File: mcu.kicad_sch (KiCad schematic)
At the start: 36 parts, among them J17 CAN, J19 Conn_ARM_JTAG_SWD_10, J20 Conn_ARM_JTAG_SWD_10, J21 Conn_01x04_Pin, SW1 RESET, SW2 BOOT, U17 HDC1080, U18 SN65HVD230, U3 STM32U575RGTx

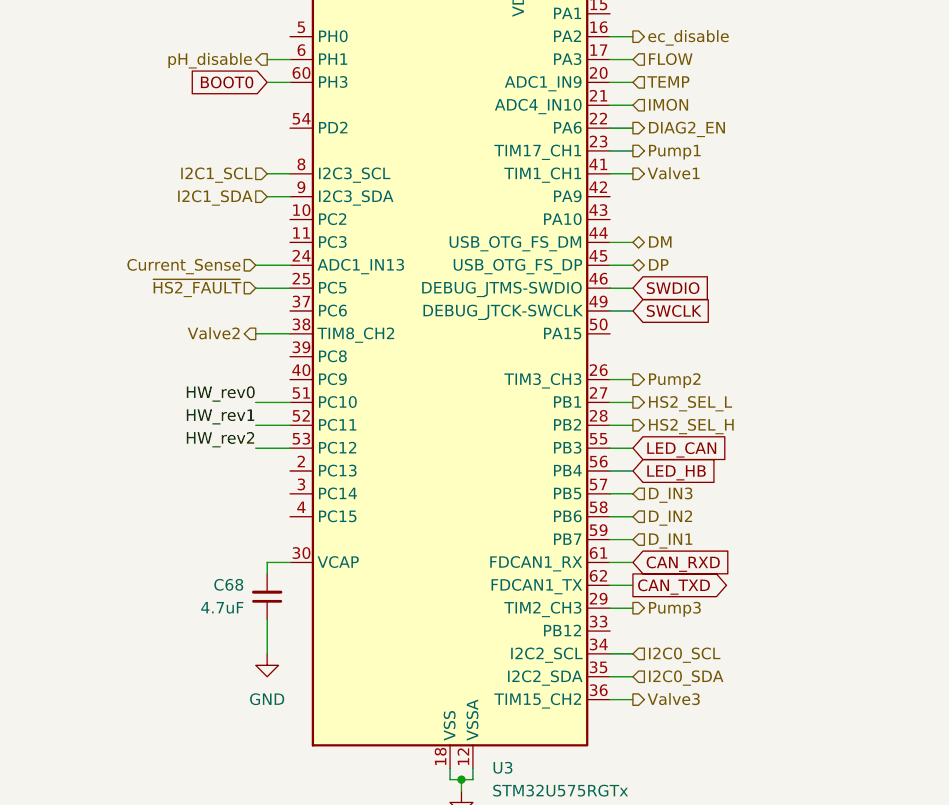
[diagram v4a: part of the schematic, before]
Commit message: Replace the last 2 of the highside outputs with TPS4H160B
Closes #50
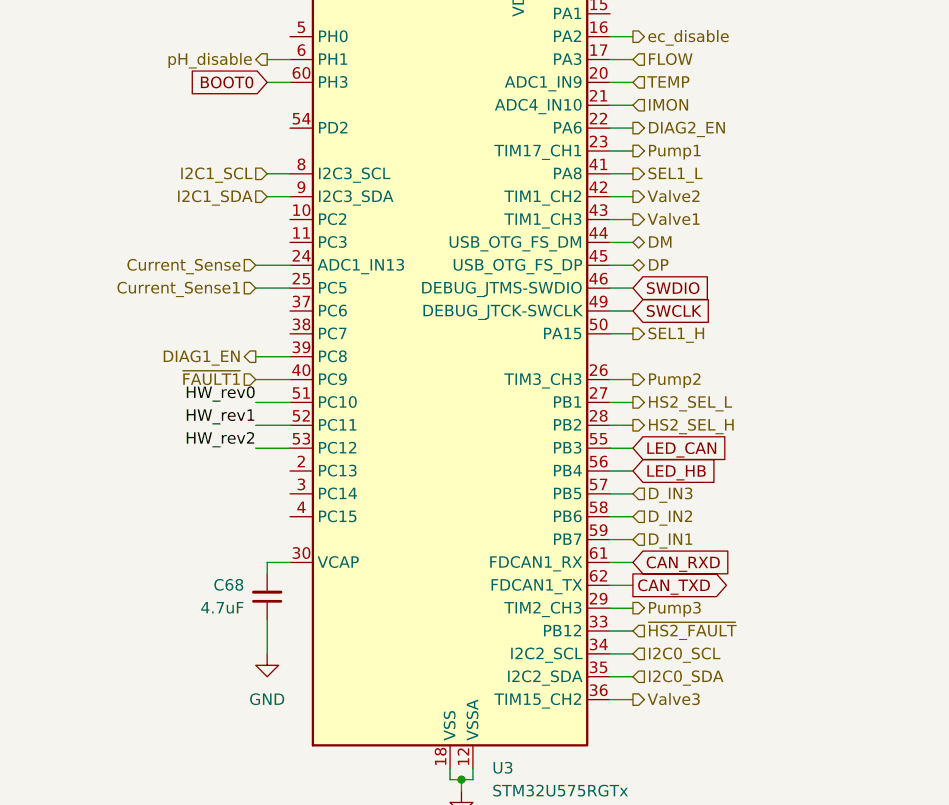
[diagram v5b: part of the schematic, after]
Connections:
- net Valve1: now also U3.43 (PA10); no longer U3.41 (PA8)
- net Valve2: now also U3.42 (PA9); no longer U3.38 (PC7)
- net ~{HS2_FAULT}: now also U3.33 (PB12); no longer U3.25 (PC5)
- net DIAG1_EN: now reaches U3.39 (PC8)
- net ~{FAULT1}: now reaches U3.40 (PC9)
- net SEL1_H: now reaches U3.50 (PA15)
- new net Current_Sense1: U3.25 (PC5)
- new net SEL1_L: U3.41 (PA8)
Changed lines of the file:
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@@
 		)
 	)
+	(wire
+		(pts
+			(xy 41.91 82.55) (xy 45.72 82.55)
+		)
+		(stroke
+			(width 0)
+			(type default)
+		)
+	)
 	(polyline
 		(pts
@@
 	(wire
 		(pts
-			(xy 41.91 77.47) (xy 45.72 77.47)
-		)
-		(stroke
-			(width 0)
-			(type default)
-		)
-	)
-	(wire
-		(pts
 			(xy 53.34 177.8) (xy 53.34 181.61)
 		)
@@
 	(wire
 		(pts
+			(xy 81.28 77.47) (xy 83.82 77.47)
+		)
+		(stroke
+			(width 0)
+			(type default)
+		)
+	)
+	(wire
+		(pts
 			(xy 43.18 59.69) (xy 45.72 59.69)
 		)
@@
 	(wire
 		(pts
+			(xy 41.91 80.01) (xy 45.72 80.01)
+		)
+		(stroke
+			(width 0)
+			(type default)
+		)
+	)
+	(wire
+		(pts
 			(xy 83.82 69.85) (xy 81.28 69.85)
 		)
@@
 	(wire
 		(pts
+			(xy 81.28 110.49) (xy 83.82 110.49)
+		)
+		(stroke
+			(width 0)
+			(type default)
+		)
+	)
+	(wire
+		(pts
 			(xy 83.82 97.79) (xy 81.28 97.79)
 		)
@@
 	(wire
 		(pts
+			(xy 81.28 62.23) (xy 83.82 62.23)
+		)
+		(stroke
+			(width 0)
+			(type default)
+		)
+	)
+	(wire
+		(pts
 			(xy 83.82 44.45) (xy 81.28 44.45)
 		)
@@
 	(wire
 		(pts
+			(xy 81.28 64.77) (xy 83.82 64.77)
+		)
+		(stroke
+			(width 0)
+			(type default)
+		)
+	)
+	(wire
+		(pts
 			(xy 63.5 125.73) (xy 63.5 127)
 		)
@@
 		)
 	)
+	(hierarchical_label "SEL1_L"
+		(shape output)
+		(at 83.82 59.69 0)
+		(effects
+			(font
+				(size 1.27 1.27)
+			)
+			(justify left)
+		)
+	)
 	(hierarchical_label "I2C0_SDA"
 		(shape input)
@@
 		)
 	)
+	(hierarchical_label "DIAG1_EN"
+		(shape output)
+		(at 41.91 80.01 180)
+		(effects
+			(font
+				(size 1.27 1.27)
+			)
+			(justify right)
+		)
+	)
 	(hierarchical_label "HS2_SEL_H"
 		(shape output)
@@
 	(hierarchical_label "~{HS2_FAULT}"
 		(shape input)
-		(at 41.91 72.39 180)
+		(at 83.82 110.49 0)
 		(effects
 			(font
 				(size 1.27 1.27)
 			)
-			(justify right)
+			(justify left)
 		)
 	)
@@
 		)
 	)
+	(hierarchical_label "~{FAULT1}"
+		(shape input)
+		(at 41.91 82.55 180)
+		(effects
+			(font
+				(size 1.27 1.27)
+			)
+			(justify right)
+		)
+	)
 	(hierarchical_label "Valve2"
 		(shape output)
-		(at 41.91 77.47 180)
+		(at 83.82 62.23 0)
 		(effects
 			(font
 				(size 1.27 1.27)
 			)
-			(justify right)
+			(justify left)
 		)
 	)
@@
 		)
 	)
+	(hierarchical_label "SEL1_H"
+		(shape output)
+		(at 83.82 77.47 0)
+		(effects
+			(font
+				(size 1.27 1.27)
+			)
+			(justify left)
+		)
+	)
 	(hierarchical_label "IMON"
 		(shape input)
@@
 	(hierarchical_label "Valve1"
 		(shape output)
-		(at 83.82 59.69 0)
+		(at 83.82 64.77 0)
 		(effects
 			(font
@@
 		)
 	)
+	(hierarchical_label "Current_Sense1"
+		(shape input)
+		(at 41.91 72.39 180)
+		(effects
+			(font
+				(size 1.27 1.27)
+			)
+			(justify right)
+		)
+	)
 	(symbol
 		(lib_id "power:+3.3V")
@@
 		)
 		(pin "38"
-			(alternate "TIM8_CH2")
+			(alternate "PC7")
 		)
 		(pin "56"
@@
 		)
 		(pin "42"
-			(alternate "PA9")
+			(alternate "TIM1_CH2")
 		)
 		(pin "29"
@@
 		)
 		(pin "43"
-			(alternate "PA10")
+			(alternate "TIM1_CH3")
 		)
 		(pin "8"
@@
 		)
 		(pin "41"
-			(alternate "TIM1_CH1")
+			(alternate "PA8")
 		)
 		(pin "26"

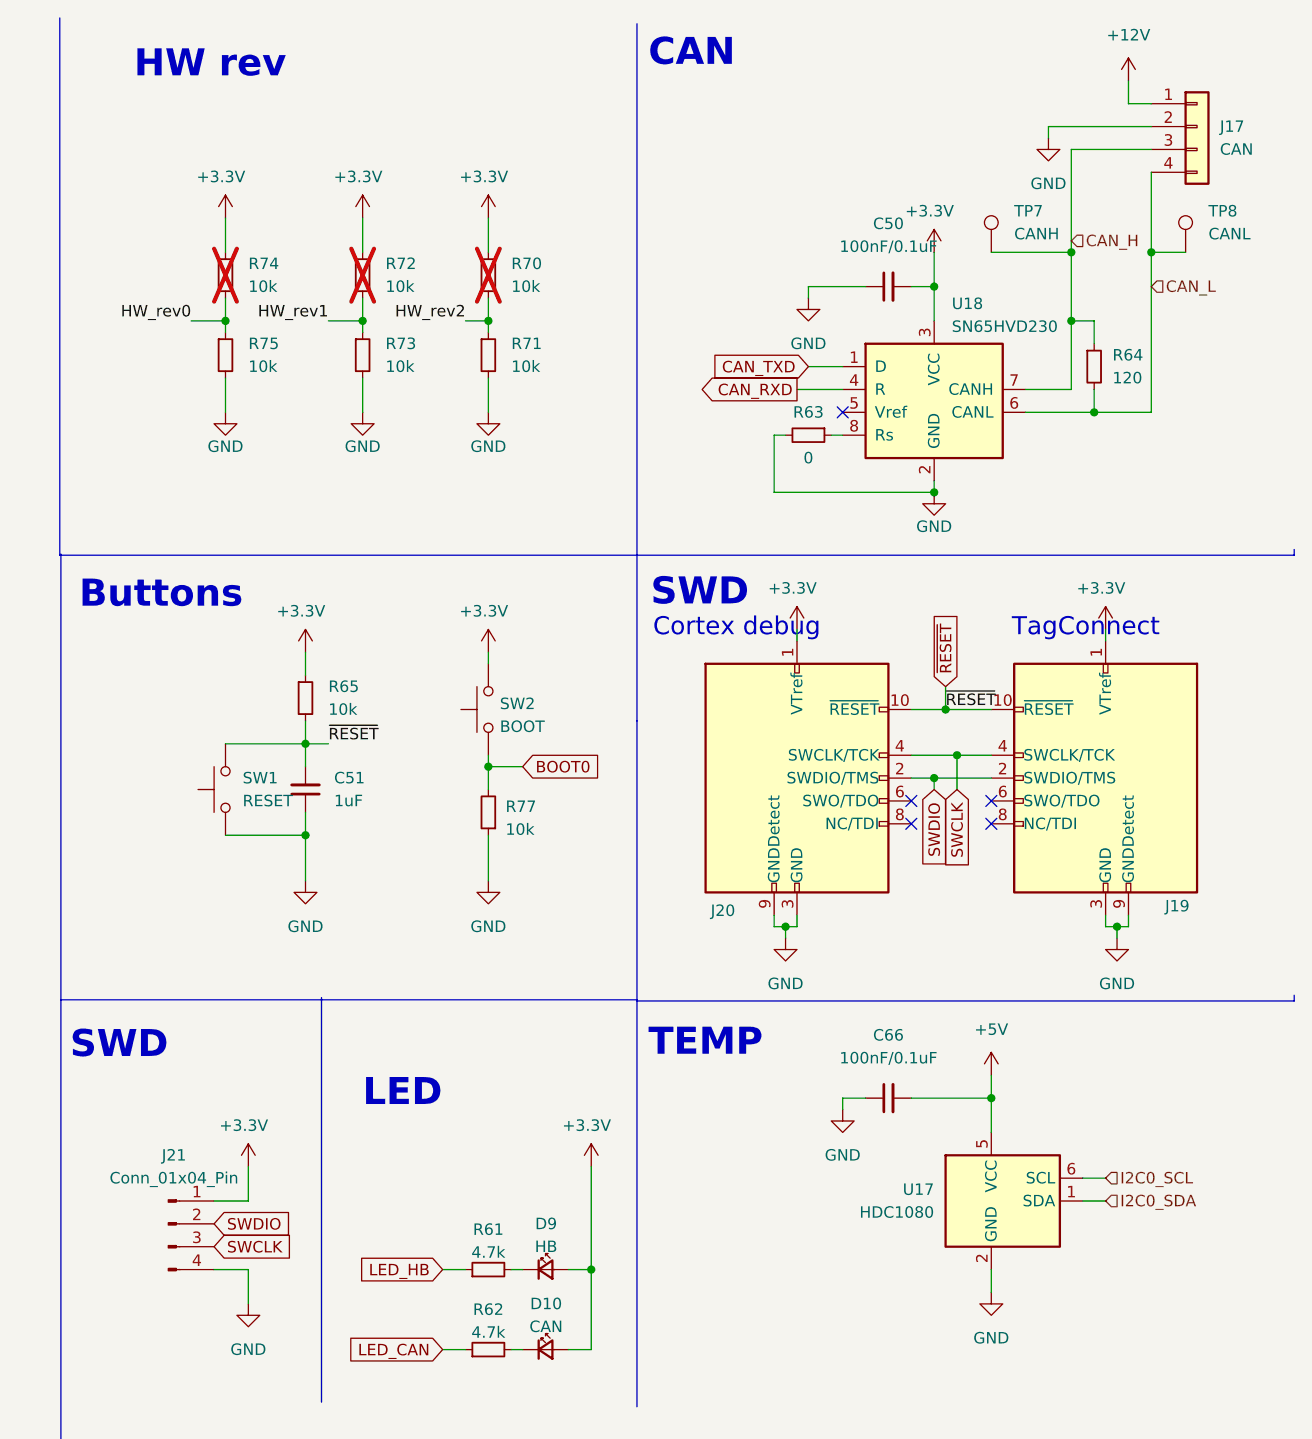
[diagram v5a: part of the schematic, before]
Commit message: Add a second CAN connector
Closes #58
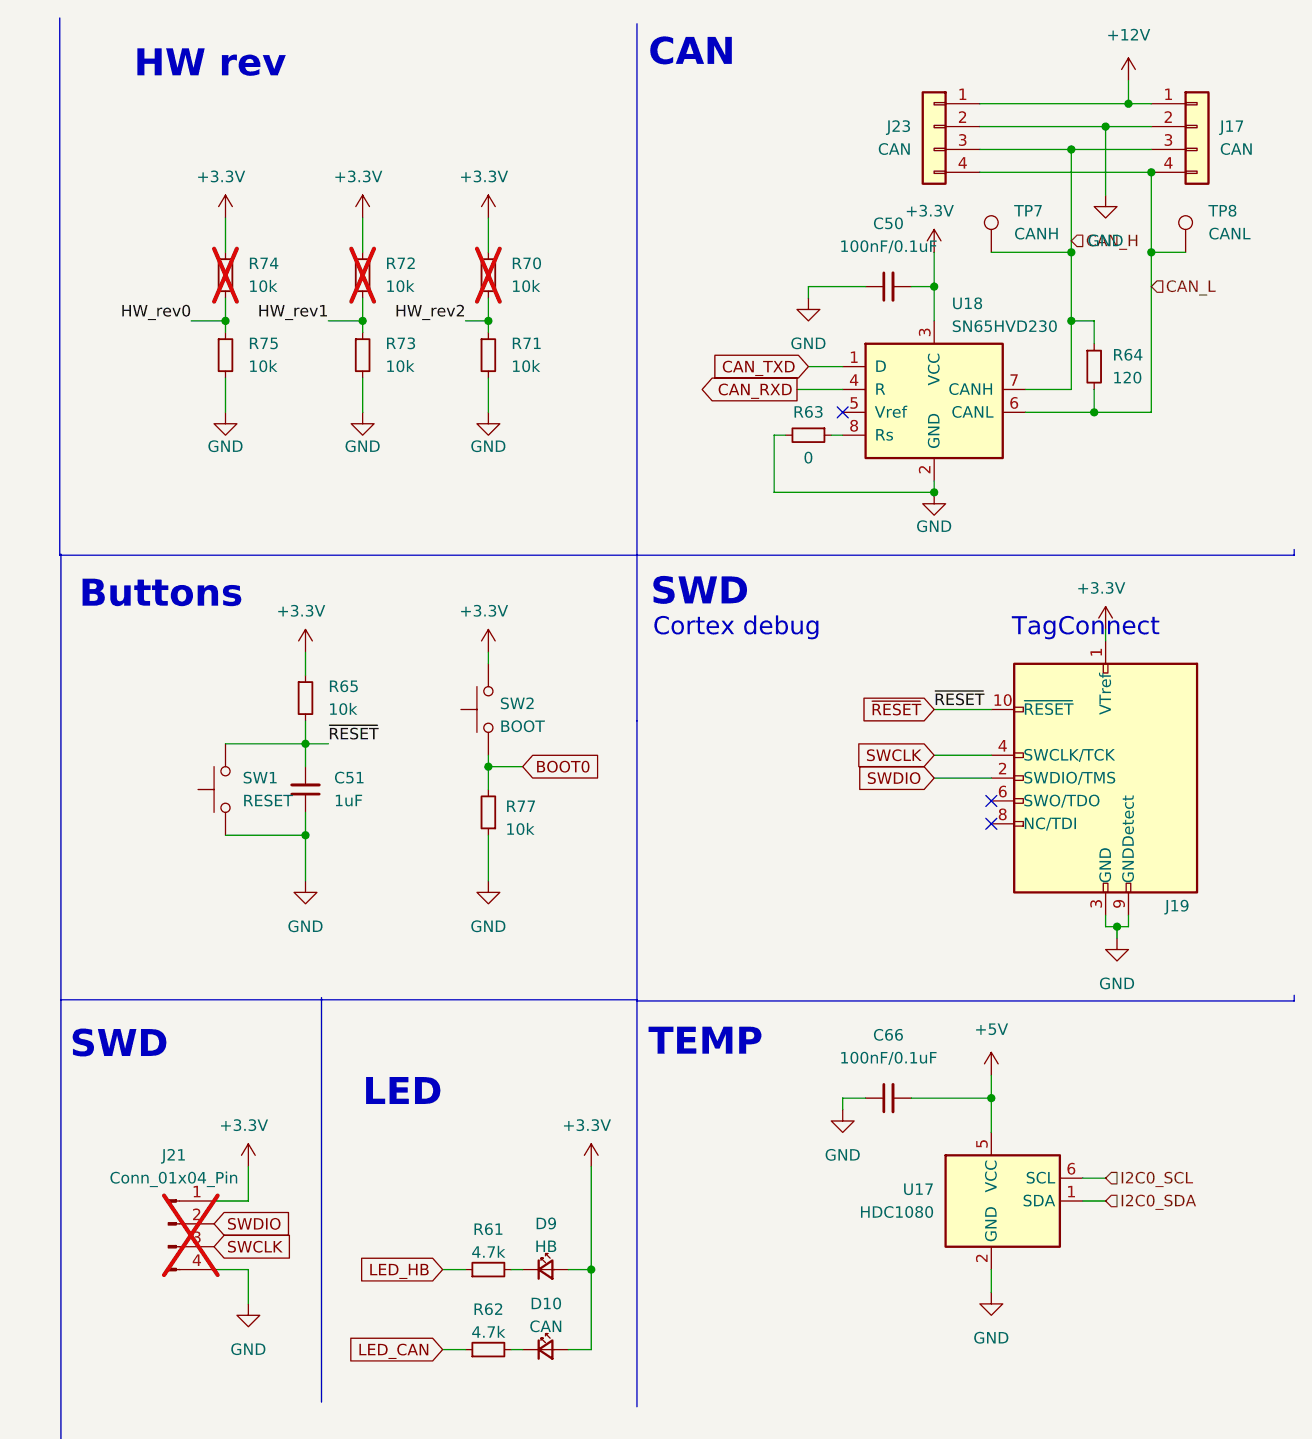
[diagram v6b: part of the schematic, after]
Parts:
- removed J20: Conn_ARM_JTAG_SWD_10, Connector_PinHeader_1.27mm:PinHeader_2x05_P1.27mm_Vertical_SMD, symbol Connector:Conn_ARM_JTAG_SWD_10
- added J23: CAN, HydroponicFlowerControl:AMASS_XT30PW(2+2), symbol Connector_Generic:Conn_01x04
- J21: now not fitted; now in the parts list
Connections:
- net +12V: now also J23.1 (Pin_1)
- net CAN_H: now also J23.3 (Pin_3)
- net CAN_L: now also J23.4 (Pin_4)
- net GND: now also J23.2 (Pin_2)
- no-connect marks 5 -> 3

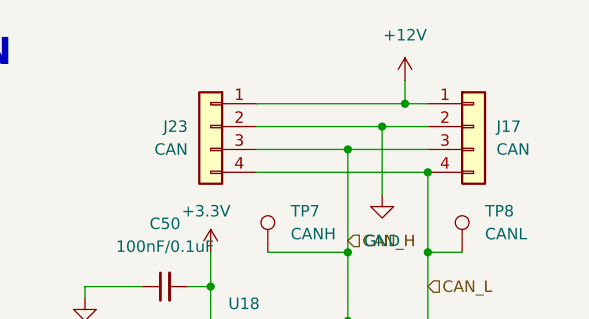
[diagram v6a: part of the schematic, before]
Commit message: Protect CAN connector from over voltage
Closes #57
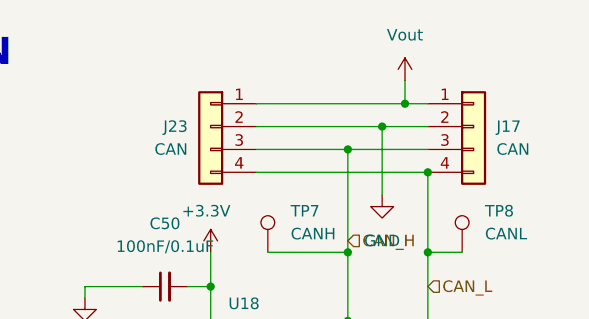
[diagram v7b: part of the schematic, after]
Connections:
- net +12V renamed Vout
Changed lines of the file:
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@@
 	)
 	(symbol
+		(lib_id "power:VDD")
+		(at 266.7 19.05 0)
+		(unit 1)
+		(exclude_from_sim no)
+		(in_bom yes)
+		(on_board yes)
+		(dnp no)
+		(fields_autoplaced yes)
+		(property "Reference" "#PWR08"
+			(at 266.7 22.86 0)
+			(effects
+				(font
+					(size 1.27 1.27)
+				)
+				(hide yes)
+			)
+		)
+		(property "Value" "Vout"
+			(at 266.7 13.97 0)
+			(effects
+				(font
+					(size 1.27 1.27)
+				)
+			)
+		)
+		(property "Footprint" ""
+			(at 266.7 19.05 0)
+			(effects
+				(font
+					(size 1.27 1.27)
+				)
+				(hide yes)
+			)
+		)
+		(property "Datasheet" ""
+			(at 266.7 19.05 0)
+			(effects
+				(font
+					(size 1.27 1.27)
+				)
+				(hide yes)
+			)
+		)
+		(property "Description" "Power symbol creates a global label with name \"Vout\""
+			(at 266.7 19.05 0)
+			(effects
+				(font
+					(size 1.27 1.27)
+				)
+				(hide yes)
+			)
+		)
+		(pin "1"
+		)
+		(instances
+			(project "HydroponicFlowerControl"
+				(path "/b3c8a28b-9ce1-4002-b8e8-ef8cb73fe031/ed65d457-d819-4893-a974-b640bac4c870"
+					(reference "#PWR08")
+					(unit 1)
+				)
+			)
+		)
+	)
+	(symbol
 		(lib_id "power:GND")
 		(at 234.95 133.35 0)
@@
 					(unit 1)
 				)
-			)
-		)
-	)
-	(symbol
-		(lib_id "power:+12V")
-		(at 266.7 19.05 0)
-		(unit 1)
-		(exclude_from_sim no)
-		(in_bom yes)
-		(on_board yes)
-		(dnp no)
-		(fields_autoplaced yes)
-		(property "Reference" "#PWR083"
-			(at 266.7 22.86 0)
-			(effects
-				(font
-					(size 1.27 1.27)
-				)
-				(hide yes)
-			)
-		)
-		(property "Value" "+12V"
-			(at 266.7 13.97 0)
-			(effects
-				(font
-					(size 1.27 1.27)
-				)
-			)
-		)
-		(property "Footprint" ""
-			(at 266.7 19.05 0)
-			(effects
-				(font
-					(size 1.27 1.27)
-				)
-				(hide yes)
-			)
-		)
-		(property "Datasheet" ""
-			(at 266.7 19.05 0)
-			(effects
-				(font
-					(size 1.27 1.27)
-				)
-				(hide yes)
-			)
-		)
-		(property "Description" "Power symbol creates a global label with name \"+12V\""
-			(at 266.7 19.05 0)
-			(effects
-				(font
-					(size 1.27 1.27)
-				)
-				(hide yes)
-			)
-		)
-		(pin "1"
-		)
-		(instances
-			(project "HydroponicFlowerControl"
-				(path "/b3c8a28b-9ce1-4002-b8e8-ef8cb73fe031/ed65d457-d819-4893-a974-b640bac4c870"
-					(reference "#PWR083")
-					(unit 1)
-				)

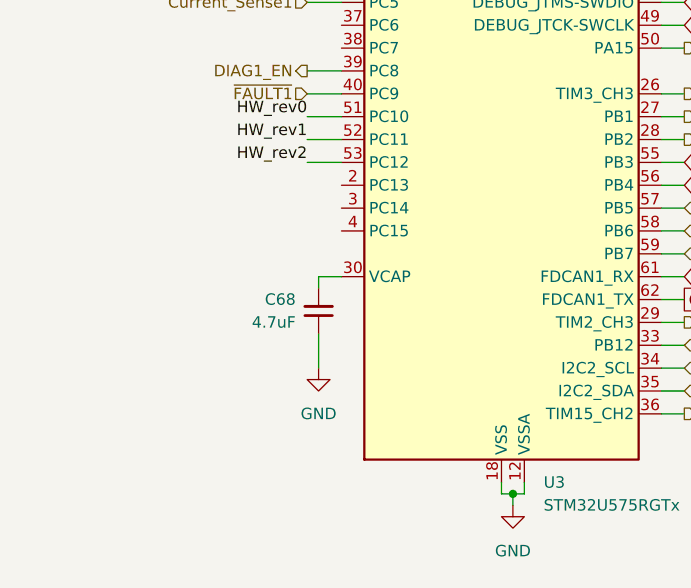
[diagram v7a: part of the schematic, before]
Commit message: Add 32kHz crystal for RTC
Closes #12
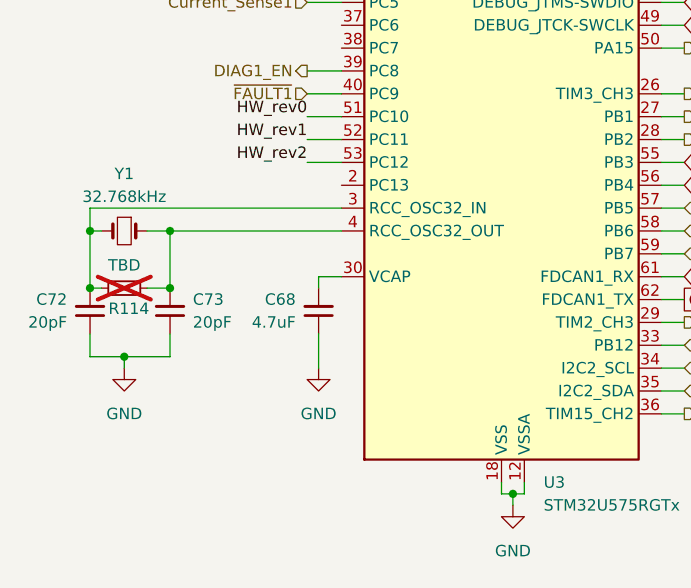
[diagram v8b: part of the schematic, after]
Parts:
- added C72, C73: 20pF, Capacitor_SMD:C_0402_1005Metric, symbol Device:C_Small
- added R114: TBD, Resistor_SMD:R_0402_1005Metric, symbol Device:R_Small
- added Y1: 32.768kHz, Crystal:Crystal_SMD_3215-2Pin_3.2x1.5mm, symbol Device:Crystal_Small
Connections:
- net GND: now also C72.1, C73.1
- net at U3.3 (PC14): now also C72.2, R114.1, Y1.2
- net at U3.4 (PC15): now also C73.2, R114.2, Y1.1
